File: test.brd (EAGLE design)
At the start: 28.9 x 20.9 mm, 16 parts

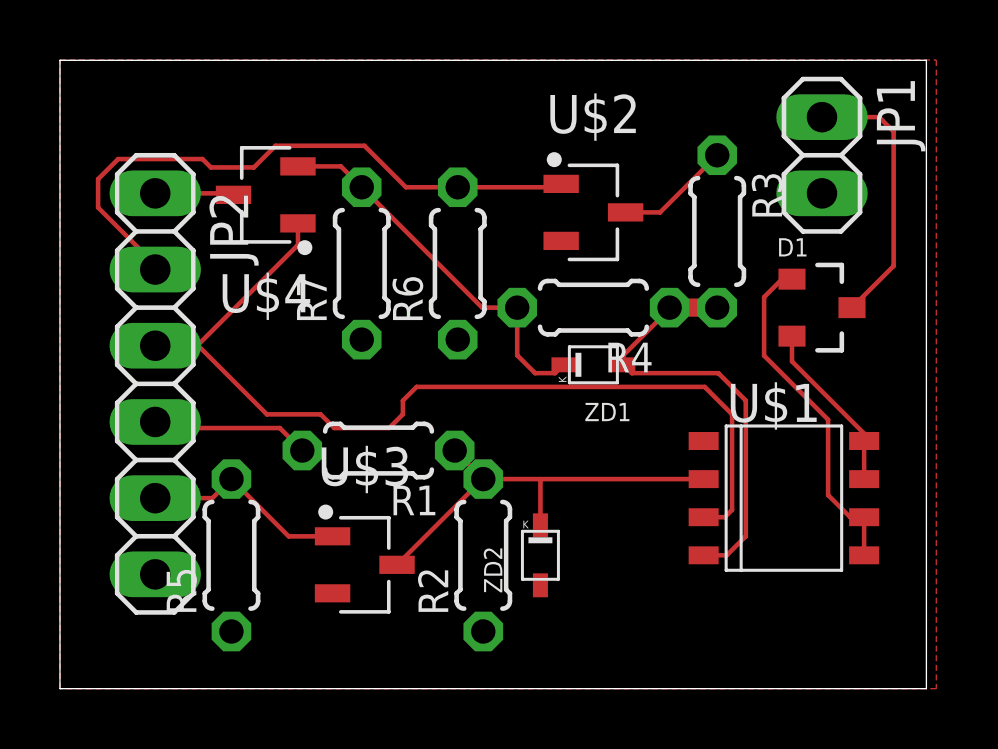
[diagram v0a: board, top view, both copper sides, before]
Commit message: removed source follower FET, which will be added on another board
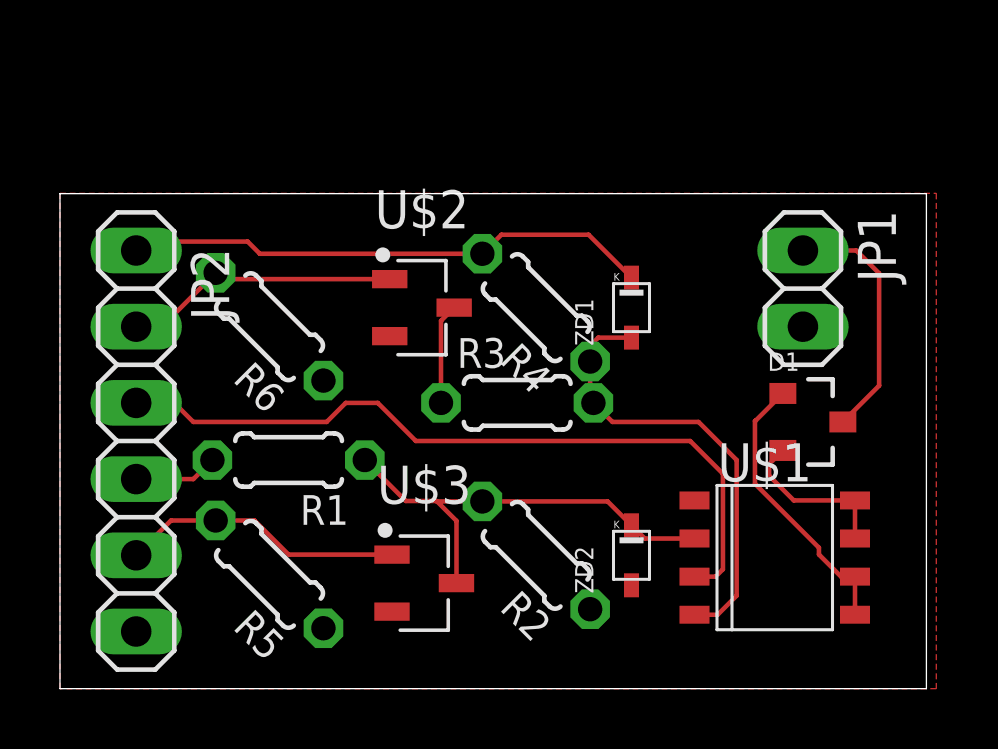
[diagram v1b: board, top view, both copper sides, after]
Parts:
- removed R7: 105, rcl:0204/5
- removed U$4: 2SK3072-TB-E, Transistor-FET:SOT95P250X120-3
- R3: value 105 -> 104
- moved R3 8.78 mm to (15.2, 9.53), turned to 0 degrees
- moved R6 6.62 mm to (6.99, 12.1), turned to 135 degrees
- moved U$2 6.54 mm to (12.1, 12.7)
- moved JP1 4.49 mm to (24.8, 13.3)
- moved D1 3.82 mm to (25.1, 8.89)
- moved ZD2 3.04 mm to (19.1, 4.45)
- moved R1 3.01 mm to (7.62, 7.62)
- moved ZD1 2.29 mm to (19.1, 12.7), turned to 0 degrees
- moved U$3 2.07 mm to (12.1, 3.52)
- moved JP2 2.01 mm to (2.54, 8.26)
- moved U$1 2.00 mm to (23.8, 4.37)
- moved R4 1.91 mm to (15.9, 12.7), turned to 135 degrees
- moved R2 1.77 mm to (15.9, 4.45), turned to 135 degrees
- moved R5 1.42 mm to (6.99, 3.81), turned to 135 degrees
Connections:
- removed net N$6: R4.2, R7.2, U$4.2, ZD1.P$1
- net GND: no longer R7.1
- net VDD: now also R4.2, ZD1.P$1; no longer U$4.3
- net VPP: no longer U$4.1
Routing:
- net VDD: track 2.63 -> 17.7 mm
- net N$6: track 12.7 -> 0.00 mm
- net N$5: track 20.5 -> 9.59 mm
- net VPP: track 31.3 -> 25.3 mm
- net N$4: track 6.96 -> 9.50 mm
- net +12V: track 5.30 -> 2.80 mm
- net N$7: track 11.4 -> 9.43 mm
- net N$1: track 14.3 -> 15.1 mm
- net N$9: track 9.03 -> 8.31 mm
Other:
- board size 28.9 x 20.9 mm -> 28.9 x 16.5 mm
